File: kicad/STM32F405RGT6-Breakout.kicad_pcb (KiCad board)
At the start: 4 copper layers, 62 parts, among them J1 USB_C_Receptacle_USB2.0, J10 Conn_01x04, J11 Conn_01x03, J2 PWR OUT, J3 SWD/JTAG, J4 USART6, J5 SPI1, J6 I2C1, J7 I2C2, J8 Conn_01x04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

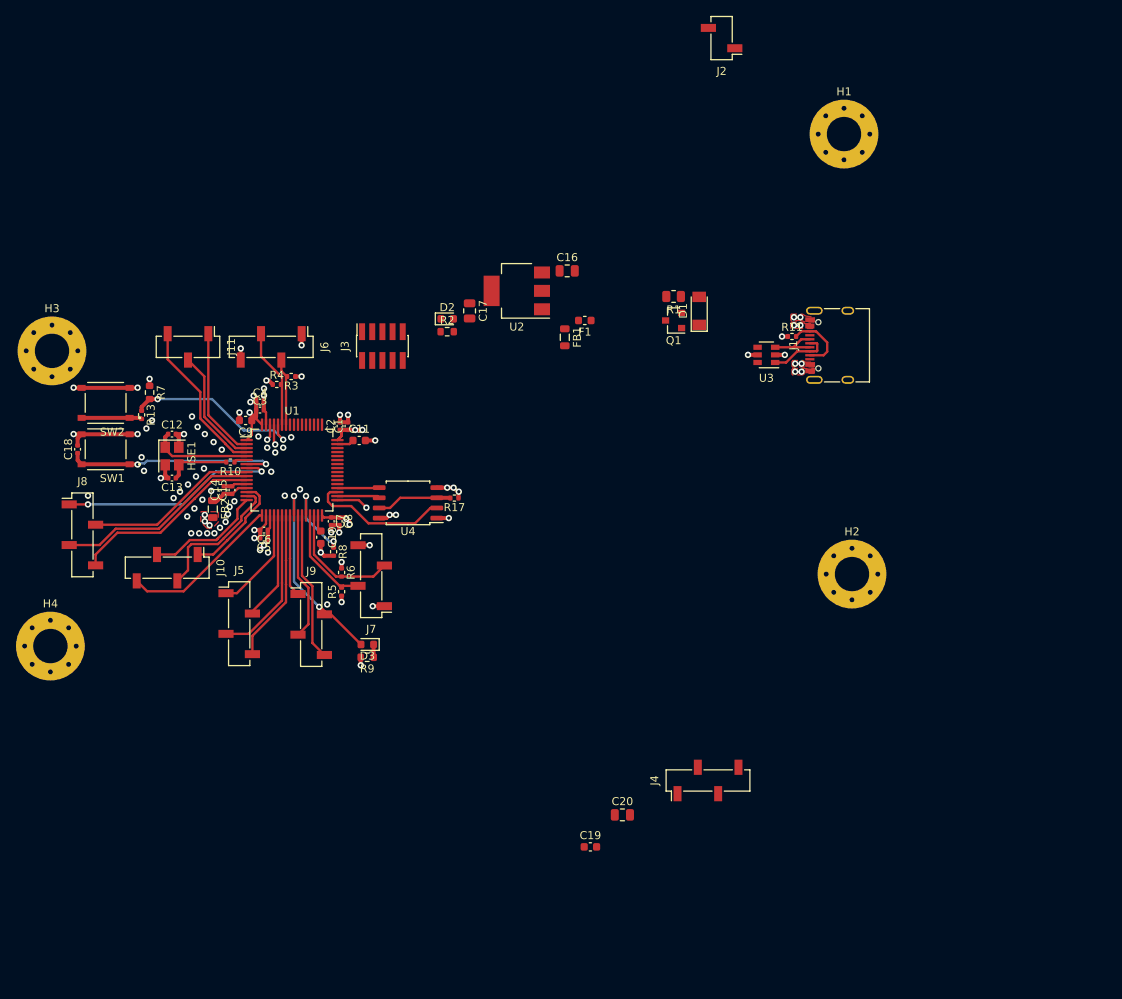
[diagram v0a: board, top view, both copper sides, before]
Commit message: - Laid out headers by Uno template - Basic functional component layout - Fixed USB connector clearances to get rid of warnings
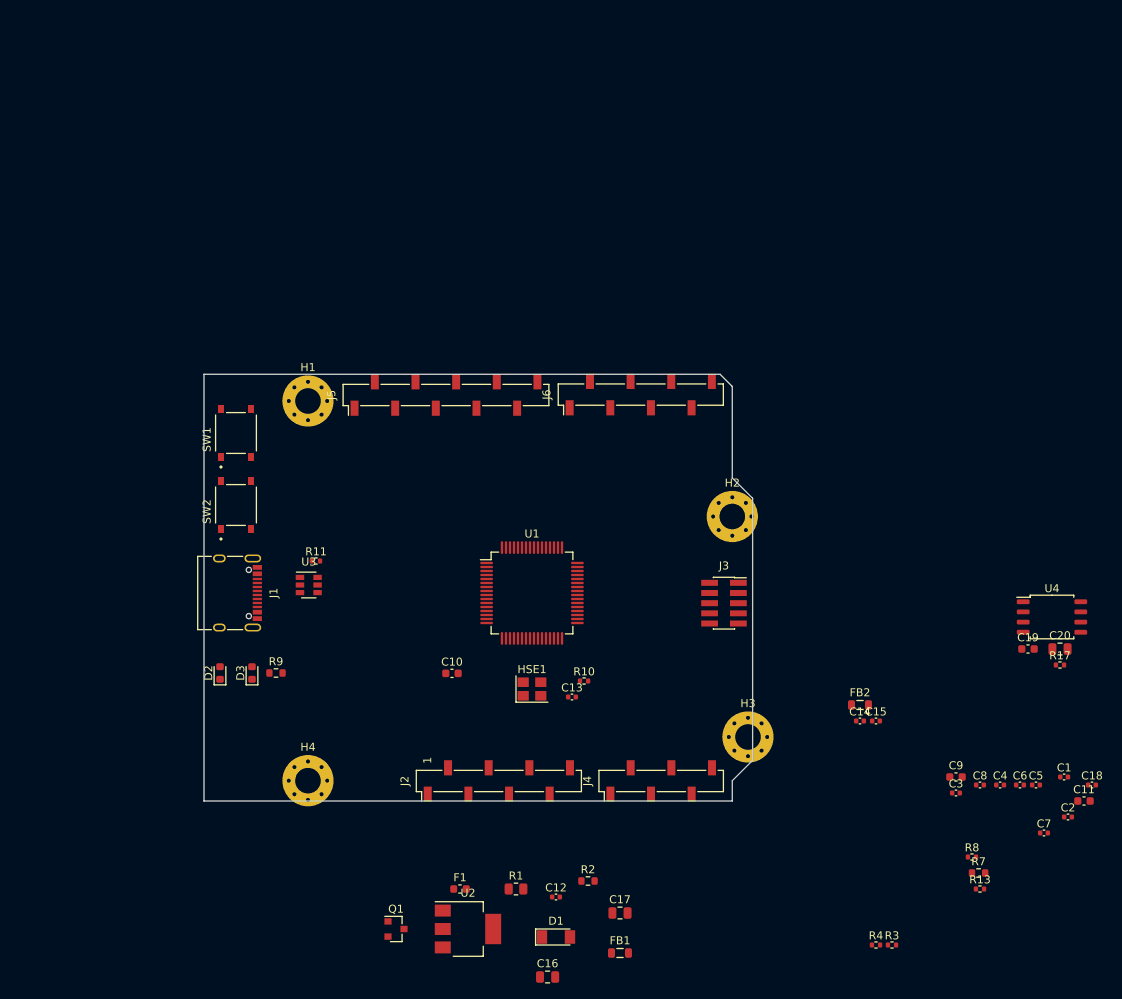
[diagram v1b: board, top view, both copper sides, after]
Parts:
- removed J10, J8, J9: Conn_01x04, Connector_PinSocket_2.54mm:PinSocket_1x04_P2.54mm_Vertical_SMD_Pin1Left
- removed J11: Conn_01x03, Connector_PinSocket_2.54mm:PinSocket_1x03_P2.54mm_Vertical_SMD_Pin1Left
- removed J7: I2C2, Connector_PinSocket_2.54mm:PinSocket_1x04_P2.54mm_Vertical_SMD_Pin1Left
- removed R5, R6: 2.2k, Resistor_SMD:R_0402_1005Metric
- H1, H2, H3, H4: footprint MountingHole:MountingHole_4.3mm_M4_Pad_Via -> MountingHole:MountingHole_3.2mm_M3_Pad_Via
- J2: value PWR OUT -> Uno Power; footprint Connector_PinSocket_2.54mm:PinSocket_1x02_P2.54mm_Vertical_SMD_Pin1Left -> Connector_PinSocket_2.54mm:PinSocket_1x08_P2.54mm_Vertical_SMD_Pin1Left
- J4: value USART6 -> Uno Analog; footprint Connector_PinSocket_2.54mm:PinSocket_1x04_P2.54mm_Vertical_SMD_Pin1Left -> Connector_PinSocket_2.54mm:PinSocket_1x06_P2.54mm_Vertical_SMD_Pin1Left
- J5: value SPI1 -> Uno Digital 2; footprint Connector_PinSocket_2.54mm:PinSocket_1x04_P2.54mm_Vertical_SMD_Pin1Left -> Connector_PinSocket_2.54mm:PinSocket_1x10_P2.54mm_Vertical_SMD_Pin1Left
- J6: value I2C1 -> Uno Digital 1; footprint Connector_PinSocket_2.54mm:PinSocket_1x04_P2.54mm_Vertical_SMD_Pin1Left -> Connector_PinSocket_2.54mm:PinSocket_1x08_P2.54mm_Vertical_SMD_Pin1Left
- moved C18 133.6 mm to (222.0, 124.4), turned to 0 degrees
- moved R13 120.4 mm to (208.0, 137.4), turned to 0 degrees
- moved R7 119.8 mm to (207.8, 135.4), turned to 0 degrees
- moved C4 104.2 mm to (210.5, 124.4)
- moved R3 103.4 mm to (197.0, 144.4), turned to 0 degrees
- moved C2 103.3 mm to (219.0, 128.4), turned to 0 degrees
- moved R4 102.6 mm to (195.0, 144.4)
- moved C5 101.3 mm to (215.0, 124.4), turned to 0 degrees
- moved C11 101.2 mm to (221.0, 126.4)
- moved C6 99.7 mm to (213.0, 124.4), turned to 0 degrees
- moved C1 99.7 mm to (218.5, 123.4), turned to 0 degrees
- moved H3 99.5 mm to (179.0, 118.4)
- moved C9 99.4 mm to (205.0, 123.4), turned to 0 degrees
- moved C3 99.3 mm to (205.0, 125.4)
- moved C7 97.2 mm to (216.0, 130.4), turned to 0 degrees
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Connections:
- J2 pad 1: GND -> Net-(J2-Pad1)
- J4 pad 1: GND -> GPIO_PC0
- J4 pad 2: USART6_TX -> GPIO_PC1
- J4 pad 3: USART6_RX -> GPIO_PC2
- J4 pad 4: +3V3 -> GPIO_PC3
- J5 pad 1: SPI1_NSS -> I2C1_SCL
- J5 pad 2: SPI1_SCK -> I2C1_SDA
- J5 pad 3: SPI1_MISO -> +3.3VA
- J5 pad 4: SPI1_MOSI -> GND
- J6 pad 1: GND -> GPIO_PC5
- J6 pad 2: I2C1_SCL -> GPIO_PC4
- J6 pad 3: I2C1_SDA -> GPIO_PA3
- J6 pad 4: +3V3 -> GPIO_PA2
- U1 pad 2: GPIO_PC13 -> Net-(U1-Pad2)
- U1 pad 26: GPIO_PB0 -> Net-(U1-Pad26)
- U1 pad 27: GPIO_PB1 -> Net-(U1-Pad27)
- U1 pad 29: I2C2_SCL -> Net-(U1-Pad29)
- U1 pad 3: GPIO_PC14 -> Net-(U1-Pad3)
- U1 pad 30: I2C2_SDA -> Net-(U1-Pad30)
- U1 pad 4: GPIO_PC15 -> Net-(U1-Pad4)
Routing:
- net GND: track 49.1 -> 0.00 mm, vias 67 -> 0
- net +3V3: track 41.4 -> 0.00 mm, vias 22 -> 0
- net GPIO_PC0: track 27.8 -> 0.00 mm, vias 2 -> 0
- net NRST: track 27.4 -> 0.00 mm, vias 2 -> 0
- net GPIO_PC2: track 25.7 -> 0.00 mm
- net GPIO_PC5: track 25.3 -> 0.00 mm, vias 2 -> 0
- net GPIO_PC3: track 24.1 -> 0.00 mm
- net BOOT0: track 22.8 -> 0.00 mm, vias 2 -> 0
- net GPIO_PC1: track 21.6 -> 0.00 mm
- net GPIO_PA3: track 20.1 -> 0.00 mm
- net GPIO_PC15: track 19.8 -> 0.00 mm
- net SPI1_MISO: track 19.4 -> 0.00 mm
- net SPI1_MOSI: track 19.1 -> 0.00 mm
- net GPIO_PB1: track 18.6 -> 0.00 mm
- net FLASH_MISO: track 17.7 -> 0.00 mm
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- removed copper zone on F.Cu, net +3V3
- removed copper zone on F.Cu, net +5V
- removed copper zone on F.Cu, net GND
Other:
- board outline added: 68.6 x 53.3 mm
- copper layers 4 -> 2
- net class 3V3 removed
- net class 5V removed
- net class Default: via_dia 0.8 -> 0.6
- board text added: "1"
- board text added: "ADC ref"
- board text added: "Boot mode"
- board text added: "Decoupling"
- board text added: "I2C"
- board text added: "PWR"
- board text added: "SPI"

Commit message: Crystal ground
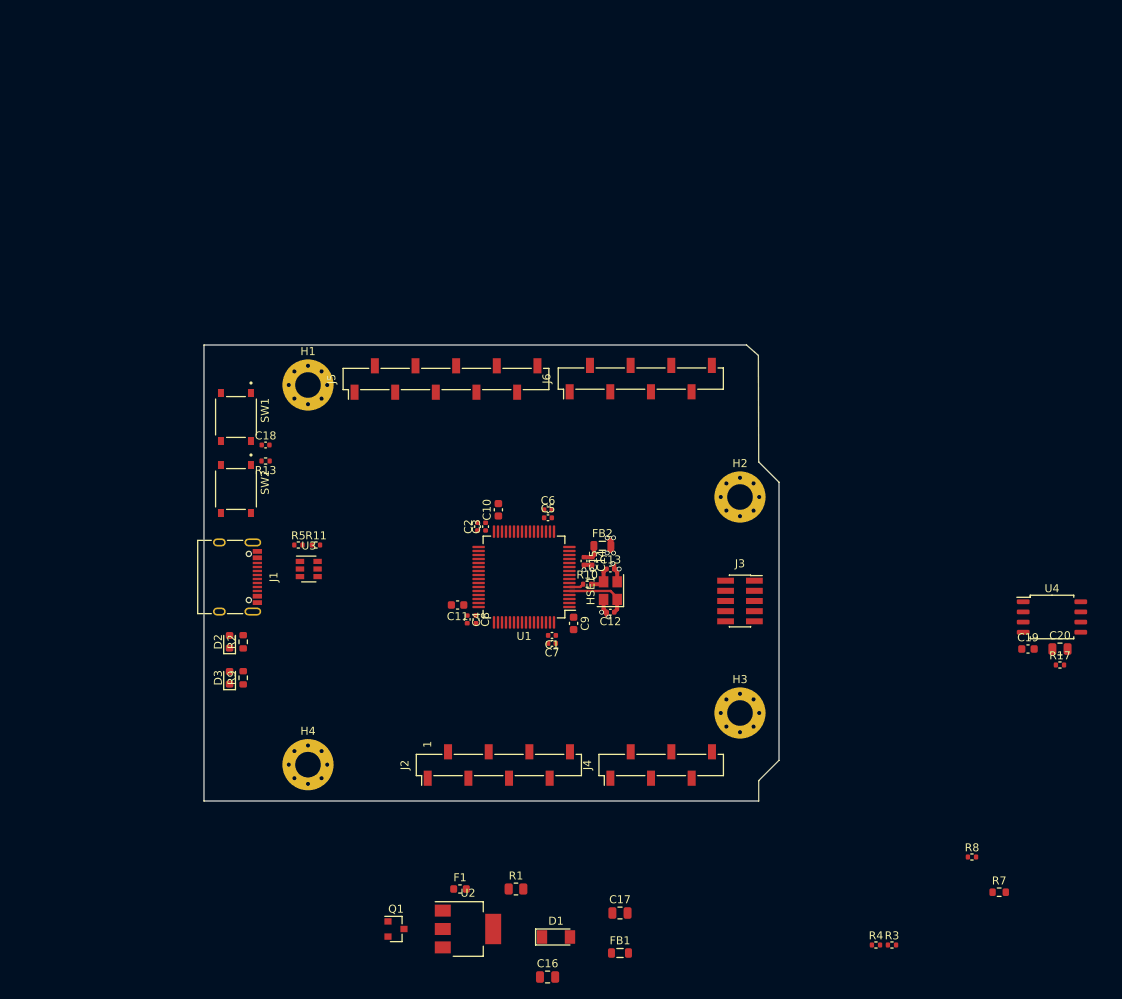
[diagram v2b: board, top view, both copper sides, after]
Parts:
- added R5: 5.1k, Resistor_SMD:R_0402_1005Metric, F.Cu at (122.8, 94.4)
- moved C18 111.7 mm to (118.7, 81.9)
- moved R13 104.1 mm to (118.7, 83.9), turned to 180 degrees
- moved C2 82.2 mm to (145.2, 92.1), turned to 90 degrees
- moved C11 82.0 mm to (142.7, 101.9), turned to 180 degrees
- moved C4 69.8 mm to (143.9, 103.7), turned to 270 degrees
- moved C5 69.5 mm to (154.0, 91.0)
- moved C6 68.3 mm to (154.0, 90.0)
- moved C3 67.6 mm to (146.2, 92.1), turned to 90 degrees
- moved C1 66.4 mm to (154.5, 105.7), turned to 180 degrees
- moved C8 66.3 mm to (145.0, 103.7), turned to 270 degrees
- moved C7 65.9 mm to (154.5, 106.7), turned to 180 degrees
- moved R2 52.5 mm to (115.9, 106.5), turned to 90 degrees
- moved C9 51.5 mm to (157.2, 104.2), turned to 270 degrees
- moved C15 41.6 mm to (158.5, 96.4), turned to 270 degrees
- moved C14 39.0 mm to (159.5, 96.4), turned to 270 degrees
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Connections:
- J1 pad B5: Net-(J1-PadA5) -> Net-(J1-PadB5)
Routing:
- net GND: track 0.00 -> 9.58 mm, vias 0 -> 6
- net HSE_IN: track 0.00 -> 8.30 mm
- net +3V3: track 0.00 -> 4.46 mm, vias 0 -> 4
- net Net-(C13-Pad1): track 0.00 -> 3.42 mm
- net +3.3VA: track 0.00 -> 2.52 mm
- net HSE_OUT: track 0.00 -> 1.86 mm
- added copper zone on In2.Cu, net +3V3
- added copper zone on In1.Cu, net GND
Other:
- board size 68.6 x 53.3 mm -> 71.9 x 57 mm
- copper layers 2 -> 4
- net class +3V3 added: clearance 0.2, trace_width 0.5, via_dia 0.6, via_drill 0.4
- net class +5V added: clearance 0.2, trace_width 0.5, via_dia 0.6, via_drill 0.4
- net class Default: trace_width 0.25 -> 0.3
- net class GND added: clearance 0.2, trace_width 0.5, via_dia 0.6, via_drill 0.4
- board text removed: "Decoupling"

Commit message: MCU decoupling
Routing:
- net GND: track 9.58 -> 37.1 mm, vias 6 -> 25
- net +3V3: track 4.46 -> 23.0 mm, vias 4 -> 13
- net Net-(C10-Pad1): track 0.00 -> 1.97 mm
- net Net-(C11-Pad1): track 0.00 -> 1.95 mm
- net +3.3VA: track 2.52 -> 4.44 mm

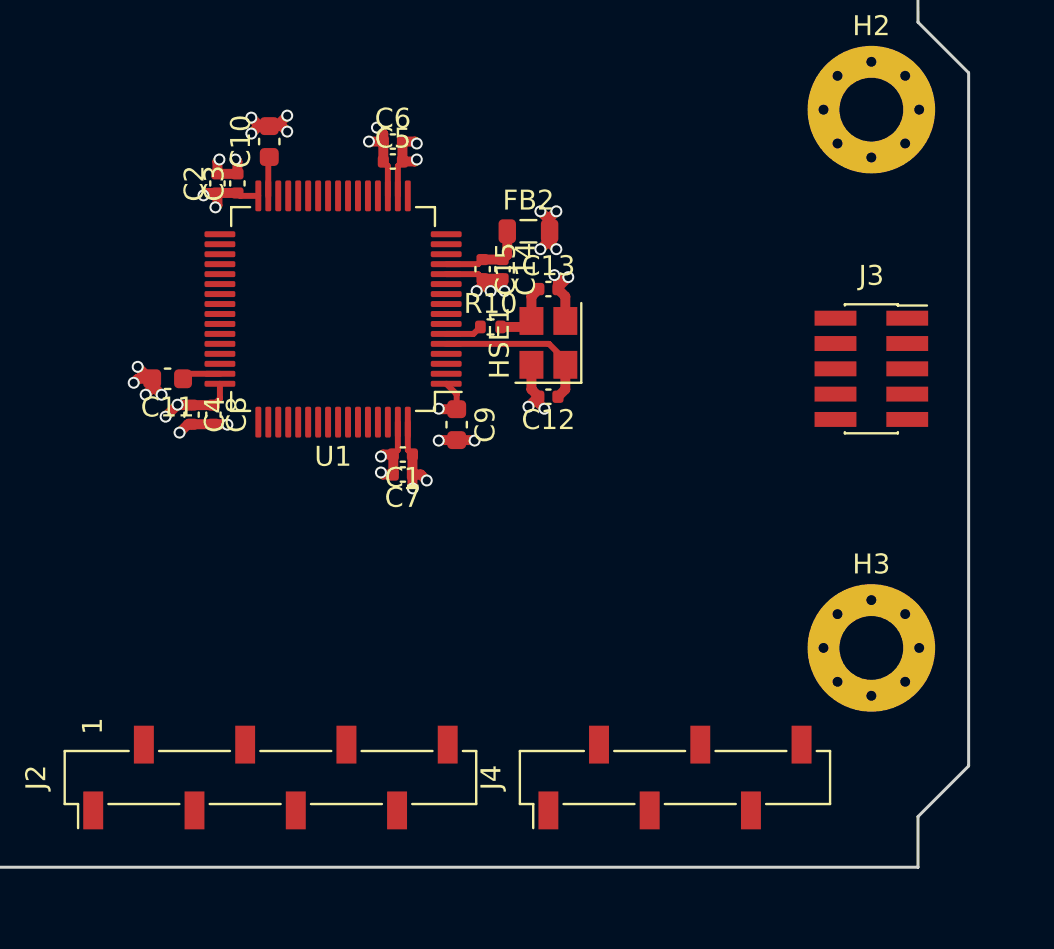
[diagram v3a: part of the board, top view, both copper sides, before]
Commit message: Start cutting out 5V plane
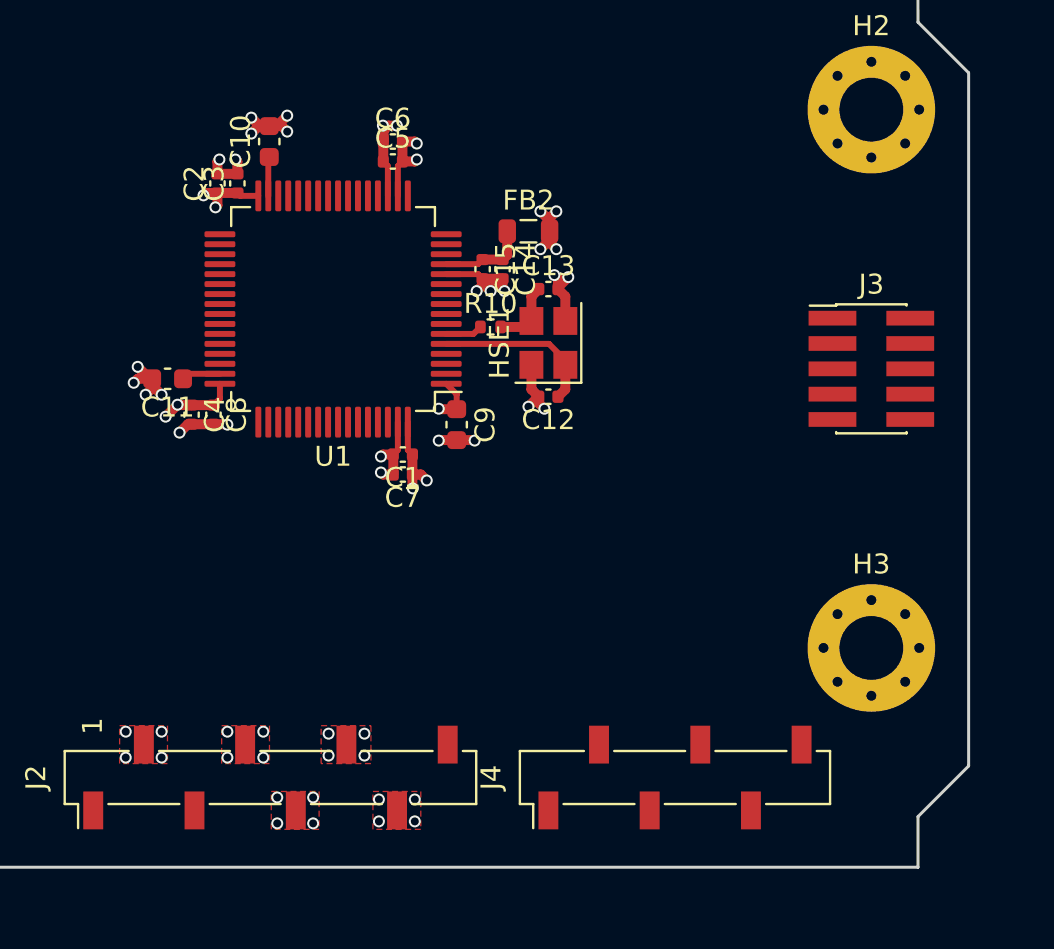
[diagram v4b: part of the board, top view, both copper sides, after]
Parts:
- J3: footprint Connector_PinSocket_1.27mm:PinSocket_2x05_P1.27mm_Vertical_SMD -> Connector_PinHeader_1.27mm:PinHeader_2x05_P1.27mm_Vertical_SMD
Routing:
- net +3V3: track 23.0 -> 23.9 mm, vias 13 -> 21
- net GND: vias 25 -> 33
- net +5V: vias 0 -> 4
- added copper zone on F.Cu, net +3V3
- added copper zone on F.Cu, net +5V
- added copper zone on F.Cu, net GND

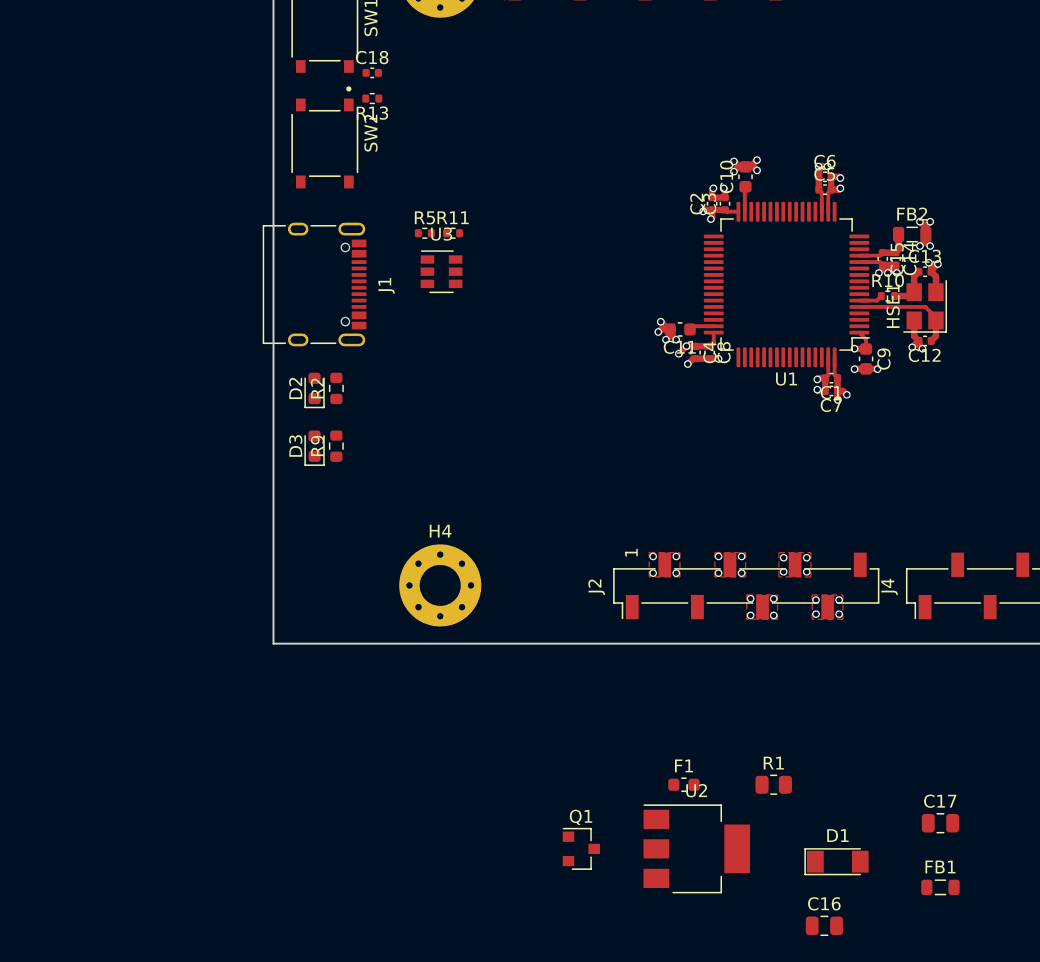
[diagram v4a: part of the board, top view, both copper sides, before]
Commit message: lol, all my via pads were too small
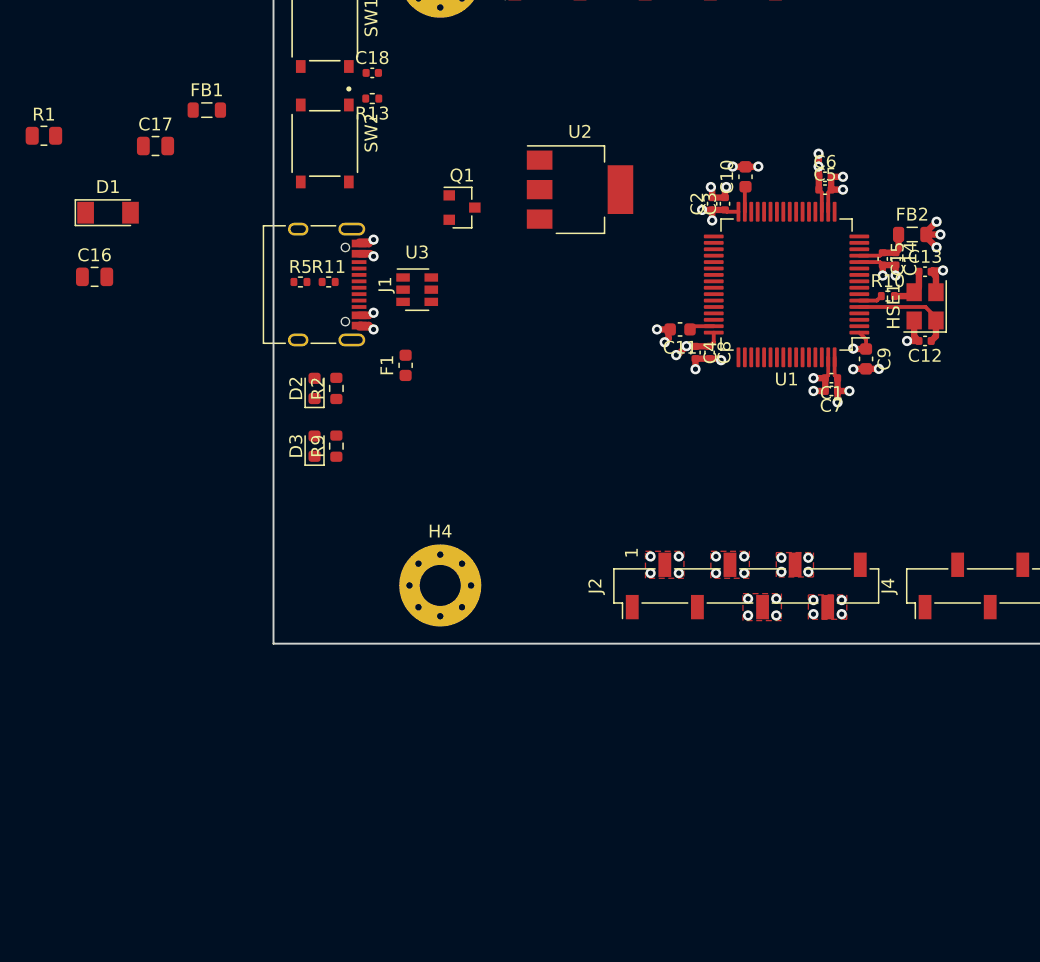
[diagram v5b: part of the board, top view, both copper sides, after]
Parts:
- moved FB1 83.3 mm to (105.8, 84.8)
- moved C17 80.8 mm to (101.8, 87.6)
- moved C16 76.1 mm to (97.0, 97.8)
- moved D1 76.1 mm to (98.1, 92.8)
- moved R1 76.1 mm to (93.1, 86.8)
- moved U2 52.2 mm to (134.9, 91.0)
- moved Q1 50.9 mm to (125.7, 92.4)
- moved F1 39.2 mm to (121.3, 104.7), turned to 90 degrees
- moved R11 10.4 mm to (115.3, 98.2)
- moved R5 10.4 mm to (113.1, 98.2)
- moved U3 2.36 mm to (122.2, 98.8)
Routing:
- net +5V: track 0.00 -> 4.85 mm, vias 4 -> 6
- net GND: track 37.1 -> 38.8 mm, vias 33 -> 28
- net +3V3: track 23.9 -> 24.7 mm, vias 21 -> 20
- added copper zone on In2.Cu, net +5V
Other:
- net class +3V3: via_dia 0.6 -> 0.8
- net class +5V: via_dia 0.6 -> 0.8
- net class Default: via_dia 0.6 -> 0.8
- net class GND: via_dia 0.6 -> 0.8
- rule via_min_drill: 0.3 -> 0.4
- rule via_min_size: 0.4 -> 0.8
